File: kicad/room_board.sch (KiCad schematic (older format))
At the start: 20 parts, among them K1 CONN_3, U1 MSP430G2452IN20, U2 7805, U3 DHT

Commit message: update files sent to osh park for board creation
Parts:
- added HDR5: AB2_HDR02-1, symbol AB2_HDR02-1
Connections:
- wire segments 70 -> 73
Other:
- moved on the sheet: K1
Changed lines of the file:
@@
 $EndComp
 $Comp
-L GND #PWR01
+L GND #PWR17
 U 1 1 541A11C0
 P 5400 3300
-F 0 "#PWR01" H 5400 3300 30  0001 C CNN
+F 0 "#PWR17" H 5400 3300 30  0001 C CNN
 F 1 "GND" H 5400 3230 30  0001 C CNN
 F 2 "" H 5400 3300 60  0000 C CNN
@@
 $EndComp
 $Comp
-L GND #PWR02
+L GND #PWR15
 U 1 1 541A11EE
 P 5150 1900
-F 0 "#PWR02" H 5150 1900 30  0001 C CNN
+F 0 "#PWR15" H 5150 1900 30  0001 C CNN
 F 1 "GND" H 5150 1830 30  0001 C CNN
 F 2 "" H 5150 1900 60  0000 C CNN
@@
 $EndComp
 $Comp
-L GND #PWR03
+L GND #PWR4
 U 1 1 541A1DFB
 P 1150 5050
-F 0 "#PWR03" H 1150 5050 30  0001 C CNN
+F 0 "#PWR4" H 1150 5050 30  0001 C CNN
 F 1 "GND" H 1150 4980 30  0001 C CNN
 F 2 "" H 1150 5050 60  0000 C CNN
@@
 $EndComp
 $Comp
-L +5V #PWR04
+L +5V #PWR1
 U 1 1 541A1E6D
 P 1000 2150
-F 0 "#PWR04" H 1000 2240 20  0001 C CNN
+F 0 "#PWR1" H 1000 2240 20  0001 C CNN
 F 1 "+5V" H 1000 2240 30  0000 C CNN
 F 2 "" H 1000 2150 60  0000 C CNN
@@
 $EndComp
 $Comp
-L +3.3V #PWR05
+L +3.3V #PWR8
 U 1 1 541A1FA0
 P 2500 2150
-F 0 "#PWR05" H 2500 2110 30  0001 C CNN
+F 0 "#PWR8" H 2500 2110 30  0001 C CNN
 F 1 "+3.3V" H 2500 2260 30  0000 C CNN
 F 2 "" H 2500 2150 60  0000 C CNN
@@
 $EndComp
 $Comp
-L GND #PWR06
+L GND #PWR7
 U 1 1 541A203B
 P 1750 2650
-F 0 "#PWR06" H 1750 2650 30  0001 C CNN
+F 0 "#PWR7" H 1750 2650 30  0001 C CNN
 F 1 "GND" H 1750 2580 30  0001 C CNN
 F 2 "" H 1750 2650 60  0000 C CNN
@@
 $EndComp
 $Comp
-L GND #PWR07
+L GND #PWR23
 U 1 1 541B579F
 P 7450 1800
-F 0 "#PWR07" H 7450 1800 30  0001 C CNN
+F 0 "#PWR23" H 7450 1800 30  0001 C CNN
 F 1 "GND" H 7450 1730 30  0001 C CNN
 F 2 "" H 7450 1800 60  0000 C CNN
@@
 $EndComp
 $Comp
-L GND #PWR08
+L GND #PWR25
 U 1 1 541B6049
 P 8350 1700
-F 0 "#PWR08" H 8350 1700 30  0001 C CNN
+F 0 "#PWR25" H 8350 1700 30  0001 C CNN
 F 1 "GND" H 8350 1630 30  0001 C CNN
 F 2 "" H 8350 1700 60  0000 C CNN
@@
 $EndComp
 $Comp
-L +3.3V #PWR09
+L +3.3V #PWR9
 U 1 1 541B7B5F
 P 2850 1700
-F 0 "#PWR09" H 2850 1660 30  0001 C CNN
+F 0 "#PWR9" H 2850 1660 30  0001 C CNN
 F 1 "+3.3V" H 2850 1810 30  0000 C CNN
 F 2 "" H 2850 1700 60  0000 C CNN
@@
 $EndComp
 $Comp
-L +3.3V #PWR010
+L +3.3V #PWR16
 U 1 1 541B7D24
 P 5400 1300
-F 0 "#PWR010" H 5400 1260 30  0001 C CNN
+F 0 "#PWR16" H 5400 1260 30  0001 C CNN
 F 1 "+3.3V" H 5400 1410 30  0000 C CNN
 F 2 "" H 5400 1300 60  0000 C CNN
@@
 $EndComp
 $Comp
-L +3.3V #PWR011
+L +3.3V #PWR21
 U 1 1 541B7FD8
 P 7300 950
-F 0 "#PWR011" H 7300 910 30  0001 C CNN
+F 0 "#PWR21" H 7300 910 30  0001 C CNN
 F 1 "+3.3V" H 7300 1060 30  0000 C CNN
 F 2 "" H 7300 950 60  0000 C CNN
@@
 $EndComp
 $Comp
-L +3.3V #PWR012
+L +3.3V #PWR24
 U 1 1 541B803D
 P 8350 1200
-F 0 "#PWR012" H 8350 1160 30  0001 C CNN
+F 0 "#PWR24" H 8350 1160 30  0001 C CNN
 F 1 "+3.3V" H 8350 1310 30  0000 C CNN
 F 2 "" H 8350 1200 60  0000 C CNN
@@
 $EndComp
 $Comp
-L +3.3V #PWR013
+L +3.3V #PWR22
 U 1 1 541B61D1
 P 7450 1400
-F 0 "#PWR013" H 7450 1360 30  0001 C CNN
+F 0 "#PWR22" H 7450 1360 30  0001 C CNN
 F 1 "+3.3V" H 7450 1510 30  0000 C CNN
 F 2 "" H 7450 1400 60  0000 C CNN
@@
 PIR_OUT
 $Comp
-L +5V #PWR014
+L +5V #PWR12
 U 1 1 5425E4B0
 P 3750 850
-F 0 "#PWR014" H 3750 940 20  0001 C CNN
+F 0 "#PWR12" H 3750 940 20  0001 C CNN
 F 1 "+5V" H 3750 940 30  0000 C CNN
 F 2 "" H 3750 850 60  0000 C CNN
@@
 $EndComp
 $Comp
-L GND #PWR015
+L GND #PWR13
 U 1 1 5425E54A
 P 3750 1100
-F 0 "#PWR015" H 3750 1100 30  0001 C CNN
+F 0 "#PWR13" H 3750 1100 30  0001 C CNN
 F 1 "GND" H 3750 1030 30  0001 C CNN
 F 2 "" H 3750 1100 60  0000 C CNN
@@
 $EndComp
 $Comp
-L GND #PWR016
+L GND #PWR27
 U 1 1 5425FC92
 P 9950 4400
-F 0 "#PWR016" H 9950 4400 30  0001 C CNN
+F 0 "#PWR27" H 9950 4400 30  0001 C CNN
 F 1 "GND" H 9950 4330 30  0001 C CNN
 F 2 "" H 9950 4400 60  0000 C CNN
@@
 $EndComp
 $Comp
-L +3.3V #PWR017
+L +3.3V #PWR26
 U 1 1 5425FE92
 P 9950 3250
-F 0 "#PWR017" H 9950 3210 30  0001 C CNN
+F 0 "#PWR26" H 9950 3210 30  0001 C CNN
 F 1 "+3.3V" H 9950 3360 30  0000 C CNN
 F 2 "" H 9950 3250 60  0000 C CNN
@@
 $EndComp
 $Comp
-L GND #PWR018
+L GND #PWR10
 U 1 1 54261CF5
 P 2850 2950
-F 0 "#PWR018" H 2850 2950 30  0001 C CNN
+F 0 "#PWR10" H 2850 2950 30  0001 C CNN
 F 1 "GND" H 2850 2880 30  0001 C CNN
 F 2 "" H 2850 2950 60  0000 C CNN
@@
 	1150 3800 1850 3800
 $Comp
-L GND #PWR019
+L GND #PWR6
 U 1 1 542639D4
-P 1600 1250
-F 0 "#PWR019" H 1600 1250 30  0001 C CNN
-F 1 "GND" H 1600 1180 30  0001 C CNN
-F 2 "" H 1600 1250 60  0000 C CNN
-F 3 "" H 1600 1250 60  0000 C CNN
-	1    1600 1250
-	1    0    0    -1
-$EndComp
-$Comp
-L +5V #PWR020
+P 1450 950
+F 0 "#PWR6" H 1450 950 30  0001 C CNN
+F 1 "GND" H 1450 880 30  0001 C CNN
+F 2 "" H 1450 950 60  0000 C CNN
+F 3 "" H 1450 950 60  0000 C CNN
+	1    1450 950
+	1    0    0    -1
+$EndComp
+$Comp
+L +5V #PWR5
 U 1 1 54263A4F
-P 1600 1000
-F 0 "#PWR020" H 1600 1090 20  0001 C CNN
-F 1 "+5V" H 1600 1090 30  0000 C CNN
-F 2 "" H 1600 1000 60  0000 C CNN
-F 3 "" H 1600 1000 60  0000 C CNN
-	1    1600 1000
-	1    0    0    -1
-$EndComp
-Wire Wire Line
-	1250 1200 1600 1200
-Wire Wire Line
-	1600 1200 1600 1250
-Wire Wire Line
-	1600 1000 1250 1000
+P 1450 700
+F 0 "#PWR5" H 1450 790 20  0001 C CNN
+F 1 "+5V" H 1450 790 30  0000 C CNN
+F 2 "" H 1450 700 60  0000 C CNN
+F 3 "" H 1450 700 60  0000 C CNN
+	1    1450 700
+	1    0    0    -1
+$EndComp
+Wire Wire Line
+	1100 900  1450 900
+Wire Wire Line
+	1450 900  1450 950
+Wire Wire Line
+	1450 700  1100 700
 $Comp
 L AB2_HDR04-2 HDR2
@@
 	3900 4700 4250 4700
 $Comp
-L GND #PWR021
+L GND #PWR11
 U 1 1 54264903
 P 3350 4450
-F 0 "#PWR021" H 3350 4450 30  0001 C CNN
+F 0 "#PWR11" H 3350 4450 30  0001 C CNN
 F 1 "GND" H 3350 4380 30  0001 C CNN
 F 2 "" H 3350 4450 60  0000 C CNN
@@
 $EndComp
 $Comp
-L +3.3V #PWR022
+L +3.3V #PWR14
 U 1 1 54264C23
 P 4250 4400
-F 0 "#PWR022" H 4250 4360 30  0001 C CNN
+F 0 "#PWR14" H 4250 4360 30  0001 C CNN
 F 1 "+3.3V" H 4250 4510 30  0000 C CNN
 F 2 "" H 4250 4400 60  0000 C CNN
@@
 TX
 $Comp
-L GND #PWR023
+L GND #PWR18
 U 1 1 5426577D
 P 5550 4550
-F 0 "#PWR023" H 5550 4550 30  0001 C CNN
+F 0 "#PWR18" H 5550 4550 30  0001 C CNN
 F 1 "GND" H 5550 4480 30  0001 C CNN
 F 2 "" H 5550 4550 60  0000 C CNN
@@
 RST
 $Comp
-L GND #PWR024
+L GND #PWR20
 U 1 1 54266071
 P 6450 4550
-F 0 "#PWR024" H 6450 4550 30  0001 C CNN
+F 0 "#PWR20" H 6450 4550 30  0001 C CNN
 F 1 "GND" H 6450 4480 30  0001 C CNN
 F 2 "" H 6450 4550 60  0000 C CNN
@@
 $EndComp
 $Comp
-L +3.3V #PWR025
+L +3.3V #PWR19
 U 1 1 54266462
 P 6250 3750
-F 0 "#PWR025" H 6250 3710 30  0001 C CNN
+F 0 "#PWR19" H 6250 3710 30  0001 C CNN
 F 1 "+3.3V" H 6250 3860 30  0000 C CNN
 F 2 "" H 6250 3750 60  0000 C CNN
@@
 L CONN_3 K1
 U 1 1 5429D710
-P 900 1100
-F 0 "K1" V 850 1100 50  0000 C CNN
-F 1 "CONN_3" V 950 1100 40  0000 C CNN
-F 2 "ab2_power:AB2_PB_2MM_JACK_PTH" H 900 1100 60  0001 C CNN
-F 3 "" H 900 1100 60  0000 C CNN
-	1    900  1100
+P 750 800
+F 0 "K1" V 700 800 50  0000 C CNN
+F 1 "CONN_3" V 800 800 40  0000 C CNN
+F 2 "ab2_power:AB2_PB_2MM_JACK_PTH" H 750 800 60  0001 C CNN
+F 3 "" H 750 800 60  0000 C CNN
+	1    750  800
 	-1   0    0    -1
 $EndComp
+$Comp
+L AB2_HDR02-1 HDR5
+U 1 1 543063E2
+P 800 1250
+F 0 "HDR5" H 800 1050 60  0000 C CNN
+F 1 "AB2_HDR02-1" H 800 1400 60  0000 C CNN
+F 2 "" H 800 1250 60  0000 C CNN
+F 3 "" H 800 1250 60  0000 C CNN
+	1    800  1250
+	1    0    0    -1
+$EndComp
+$Comp
+L GND #PWR3
+U 1 1 54306686
+P 1150 1400
+F 0 "#PWR3" H 1150 1400 30  0001 C CNN
+F 1 "GND" H 1150 1330 30  0001 C CNN
+F 2 "" H 1150 1400 60  0000 C CNN
+F 3 "" H 1150 1400 60  0000 C CNN
+	1    1150 1400
+	1    0    0    -1
+$EndComp
+$Comp
+L +5V #PWR2
+U 1 1 5430668C
+P 1150 1250
+F 0 "#PWR2" H 1150 1340 20  0001 C CNN
+F 1 "+5V" H 1150 1340 30  0000 C CNN
+F 2 "" H 1150 1250 60  0000 C CNN
+F 3 "" H 1150 1250 60  0000 C CNN
+	1    1150 1250
+	1    0    0    -1
+$EndComp
+Wire Wire Line
+	800  1350 1150 1350
+Wire Wire Line
+	1150 1350 1150 1400
+Wire Wire Line
+	1150 1250 800  1250
 $EndSCHEMATC

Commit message: update kicad schematic
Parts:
- removed U1: MSP430G2452IN20, Sockets_DIP:DIP-20__300, symbol MSP430G2452IN20
- added U1: MSP430G2553IN20, Sockets_DIP:DIP-20__300, symbol MSP430G2553IN20
- HDR2: value AB2_HDR04-2 -> NRF24L01
- HDR4: value AB2_HDR03-1 -> PROGRAM
- HDR5: value AB2_HDR02-1 -> POWER; footprint (none) -> ab2_header:AB2_HDR_M02-1V
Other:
- note removed: "NRF24L01\n"
- moved on the sheet: C1

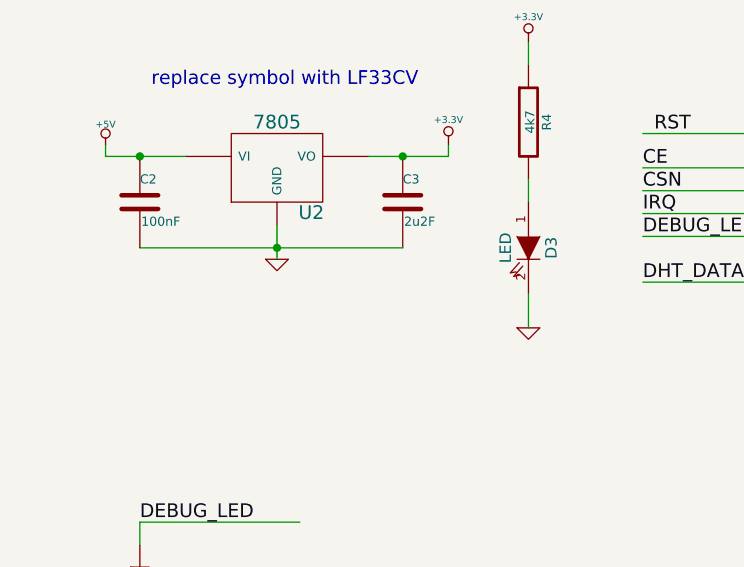
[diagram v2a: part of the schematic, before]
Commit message: schematic: add todo to change c3
According to the datasheet of the lm33cv c3 has to be an electrolyt capacitor and not a default capacitor.
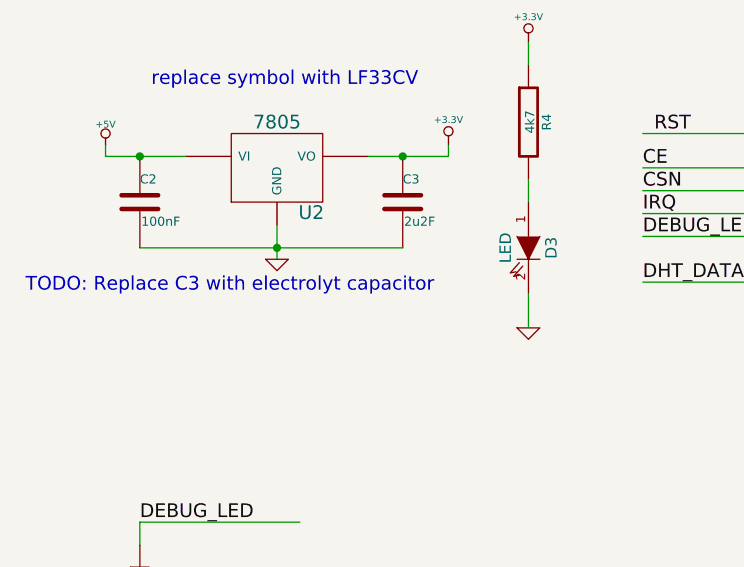
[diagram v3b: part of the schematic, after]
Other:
- note added: "TODO: Replace C3 with electrolyt capacitor"
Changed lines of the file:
@@
 Wire Wire Line
 	5350 1800 5350 1900
+Text Notes 650  2800 0    60   ~ 0
+TODO: Replace C3 with electrolyt capacitor
 $EndSCHEMATC

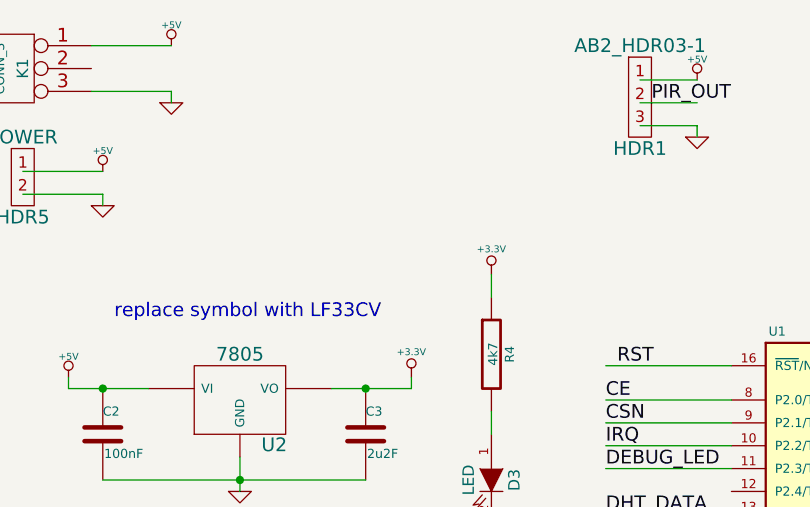
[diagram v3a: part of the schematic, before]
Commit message: add jumper for power led
Enable possibility to turn off power led to reduce power consumption when using a battery.
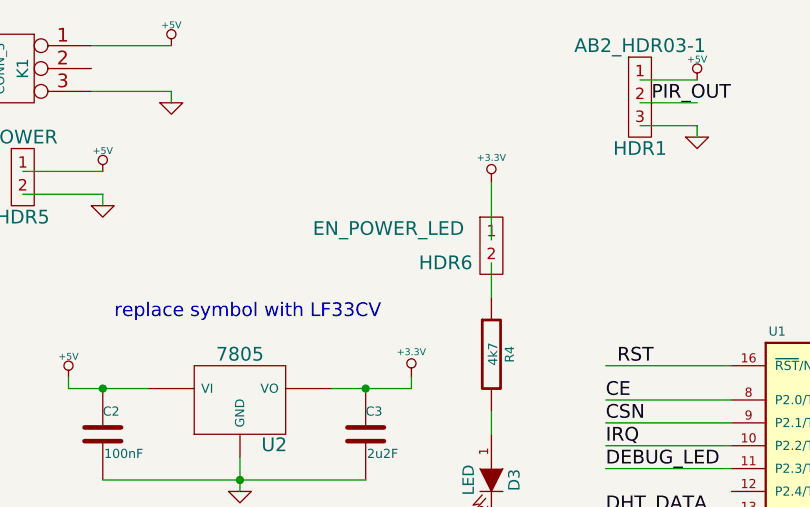
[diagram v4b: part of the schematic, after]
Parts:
- added HDR6: EN_POWER_LED, ab2_header:AB2_HDR_M02-1V, symbol AB2_HDR02-1
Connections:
- wire segments 73 -> 74
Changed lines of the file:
@@
 L +3.3V #PWR09
 U 1 1 541B7B5F
-P 2850 1700
-F 0 "#PWR09" H 2850 1660 30  0001 C CNN
-F 1 "+3.3V" H 2850 1810 30  0000 C CNN
-F 2 "" H 2850 1700 60  0000 C CNN
-F 3 "" H 2850 1700 60  0000 C CNN
-	1    2850 1700
+P 2850 1300
+F 0 "#PWR09" H 2850 1260 30  0001 C CNN
+F 1 "+3.3V" H 2850 1410 30  0000 C CNN
+F 2 "" H 2850 1300 60  0000 C CNN
+F 3 "" H 2850 1300 60  0000 C CNN
+	1    2850 1300
 	1    0    0    -1
 $EndComp
@@
 	2850 2400 2850 2300
 Wire Wire Line
-	2850 1800 2850 1700
+	2850 1650 2850 1800
 Text Label 1150 3800 0    60   ~ 0
 DEBUG_LED
@@
 Text Notes 650  2800 0    60   ~ 0
 TODO: Replace C3 with electrolyt capacitor
+$Comp
+L AB2_HDR02-1 HDR6
+U 1 1 5470ACF4
+P 2850 1550
+F 0 "HDR6" H 2650 1450 60  0000 C CNN
+F 1 "EN_POWER_LED" H 2400 1600 60  0000 C CNN
+F 2 "ab2_header:AB2_HDR_M02-1V" H 2850 1550 60  0001 C CNN
+F 3 "" H 2850 1550 60  0000 C CNN
+	1    2850 1550
+	1    0    0    -1
+$EndComp
+Wire Wire Line
+	2850 1300 2850 1550
 $EndSCHEMATC

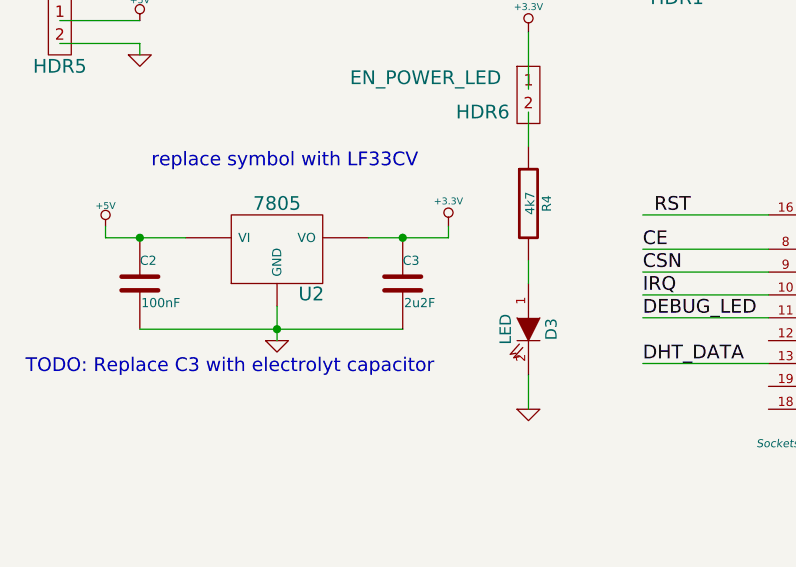
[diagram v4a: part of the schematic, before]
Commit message: replace capacitory with electrolytic version
The LCV33CV needs an electrolytic capacitor on it's output.
Fix in schematic and pcb.
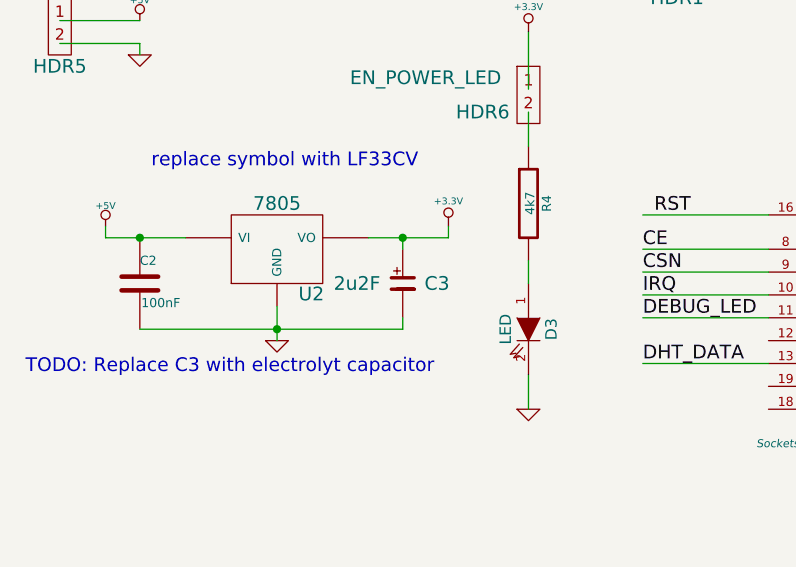
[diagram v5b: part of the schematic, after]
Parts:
- removed C3: 2u2F, Discret:C1, symbol C
- added C3: 2u2F, Capacitors_Elko_ThroughHole:Elko_vert_11x5mm_RM2.5, symbol AB2_C-POL
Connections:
- wire segments 74 -> 76
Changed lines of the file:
@@
-$EndComp
-$Comp
-L C C3
-U 1 1 541A1A92
-P 2300 2400
-F 0 "C3" H 2300 2500 40  0000 L CNN
-F 1 "2u2F" H 2306 2315 40  0000 L CNN
-F 2 "Discret:C1" H 2338 2250 30  0001 C CNN
-F 3 "" H 2300 2400 60  0000 C CNN
-	1    2300 2400
-	1    0    0    -1
 $EndComp
 $Comp
@@
 Wire Wire Line
 	2850 1300 2850 1550
+$Comp
+L AB2_C-POL C3
+U 1 1 5482F1D6
+P 2300 2400
+F 0 "C3" V 2300 2250 60  0000 C CNN
+F 1 "2u2F" V 2300 2600 60  0000 C CNN
+F 2 "Capacitors_Elko_ThroughHole:Elko_vert_11x5mm_RM2.5" H 2300 2400 60  0001 C CNN
+F 3 "" H 2300 2400 60  0000 C CNN
+	1    2300 2400
+	0    -1   -1   0
+$EndComp
+Wire Wire Line
+	2300 2250 2300 2200
+Wire Wire Line
+	2300 2600 2300 2550
 $EndSCHEMATC
